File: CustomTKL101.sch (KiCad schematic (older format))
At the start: 223 parts

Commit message: fixed global flags
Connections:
- net DB+ is gone; now on net D+: R?.2
- net DB- is gone; now on net D-: R?.2
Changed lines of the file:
@@
 	4800 8200 4500 8200
 Text GLabel 4500 8200 0    50   Input ~ 0
-DB-
+D-
 $Comp
 L Device:R_Small R?
@@
 	5300 8000 5350 8000
 Text GLabel 4500 8000 0    50   Input ~ 0
-DB+
+D+
 Wire Wire Line
 	4500 8000 4800 8000

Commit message: Board Progress
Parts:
- C1, C2, C3, C4, C5, C6, C7: renamed from C?; footprint (none) -> Capacitor_SMD:C_0805_2012Metric
- D1, D10, D100, D101, D11, D12, D13, D14, D15, D16, D17, D18, D19, D2, D20, D21, D22, D23, D24, D25, D26, D27, D28, D29, D3, D30, D31, D32, D33, D34, D35, D36, D37, D38, D39, D4, D40, D41, D42, D43, D44, D45, D46, D47, D48, D49, D5, D50, D51, D52, D53, D54, D55, D56, D57, D58, D59, D6, D60, D61, D62, D63, D64, D65, D66, D67, D68, D69, D7, D70, D71, D72, D73, D74, D75, D76, D77, D78, D79, D8, D80, D81, D82, D83, D84, D85, D86, D87, D88, D89, D9, D90, D91, D92, D93, D94, D95, D96, D97, D98, D99: renamed from D?; footprint (none) -> Diode_SMD:D_SOD-123
- F1: renamed from F?; footprint (none) -> Fuse:Fuse_1206_3216Metric
- J1: renamed from J?; footprint GCT_USB4085-GF-A_REVA -> USB4085-GF-A_REVA:GCT_USB4085-GF-A_REVA
- MX1, MX10, MX100, MX101, MX11, MX12, MX13, MX14, MX15, MX16, MX17, MX18, MX19, MX2, MX20, MX21, MX22, MX23, MX24, MX25, MX26, MX27, MX28, MX29, MX3, MX30, MX31, MX32, MX33, MX34, MX35, MX36, MX37, MX38, MX39, MX4, MX40, MX41, MX42, MX43, MX44, MX45, MX46, MX47, MX48, MX49, MX5, MX50, MX51, MX52, MX53, MX54, MX55, MX56, MX57, MX58, MX59, MX6, MX60, MX61, MX62, MX63, MX64, MX65, MX66, MX67, MX68, MX69, MX7, MX70, MX71, MX72, MX73, MX74, MX75, MX76, MX77, MX78, MX79, MX8, MX80, MX81, MX82, MX83, MX84, MX85, MX86, MX87, MX88, MX89, MX9, MX90, MX91, MX92, MX93, MX94, MX95, MX96, MX97, MX98, MX99: renamed from MX?; footprint (none) -> MX_Alps_Hybrid:MX-1U-NoLED
- R1, R2, R3, R4, R5, R6, R7, R8, R9: renamed from R?; footprint (none) -> Resistor_SMD:R_0805_2012Metric
- SW1: renamed from SW?; footprint (none) -> random-keyboard-parts:SKQG-1155865
- Y1: renamed from Y?; footprint (none) -> Crystal:Crystal_SMD_3225-4Pin_3.2x2.5mm
- gave numbers to parts that had none: 1

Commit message: Board Complete
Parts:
- removed R2: 1.5k, Resistor_SMD:R_0805_2012Metric, symbol Device:R_Small
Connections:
- net Col0&1: now also U1.41 (PF0)
- net Col10&11: now also U1.12 (PB7)
- net Col12&13: now also U1.22 (PD5)
- net Col14&15: now also U1.21 (PD3)
- net Col16&17: now also U1.20 (PD2)
- net Col18&19: now also U1.19 (PD1)
- net Col2&3: now also U1.8 (PB0)
- net Col20: now also MX36.1 (COL), U1.18 (PD0)
- net Col4&5: now also U1.9 (PB1)
- net Col6&7: now also U1.10 (PB2)
- net Col8&9: now also U1.11 (PB3)
- net GND: now also J1.P1 (SHELL), J1.P2 (SHELL), J1.P3 (SHELL), J1.P4 (SHELL)
- net Row0.1: now also U1.25 (PD4)
- net Row0.2: now also U1.26 (PD6)
- net Row1.1: now also U1.40 (PF1)
- net Row1.2: now also U1.32 (PC7)
- net Row2.1: now also U1.39 (PF4)
- net Row2.2: now also U1.31 (PC6)
- net Row3.1: now also U1.38 (PF5)
- net Row3.2: now also U1.30 (PB6)
- net Row4.1: now also U1.37 (PF6)
- net Row4.2: now also U1.29 (PB5)
- net Row5.1: now also U1.36 (PF7)
- net Row5.2: now also U1.28 (PB4)
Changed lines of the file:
@@
 $EndComp
 Wire Wire Line
-	5150 8700 5350 8700
+	5150 8700 5250 8700
 $Comp
 L Device:R_Small R6
@@
 	1    0    0    -1
 $EndComp
-Connection ~ 4500 7600
-Wire Wire Line
-	4500 7600 4450 7600
-Wire Wire Line
-	4800 7600 4500 7600
-$Comp
-L Device:R_Small R2
-U 1 1 5E4AC4C3
-P 4500 7500
-F 0 "R2" H 4300 7600 50  0000 L CNN
-F 1 "1.5k" H 4300 7500 50  0000 L CNN
-F 2 "Resistor_SMD:R_0805_2012Metric" H 4500 7500 50  0001 C CNN
-F 3 "~" H 4500 7500 50  0001 C CNN
-	1    4500 7500
-	1    0    0    -1
-$EndComp
-$Comp
-L power:+5V #PWR0114
-U 1 1 5E4AFBE5
-P 4500 7400
-F 0 "#PWR0114" H 4500 7250 50  0001 C CNN
-F 1 "+5V" H 4515 7573 50  0000 C CNN
-F 2 "" H 4500 7400 50  0001 C CNN
-F 3 "" H 4500 7400 50  0001 C CNN
-	1    4500 7400
-	1    0    0    -1
-$EndComp
 $Comp
 L power:+5V #PWR0115
@@
 	9900 1400 9900 2450
 Wire Wire Line
-	15100 1150 15100 3200
+	15100 1150 15100 2450
 Wire Wire Line
 	12250 4400 14850 4400
@@
 Wire Wire Line
 	4250 9650 4500 9650
+Wire Wire Line
+	5350 8600 5250 8600
+Wire Wire Line
+	5250 8600 5250 8700
+Connection ~ 5250 8700
+Wire Wire Line
+	5250 8700 5350 8700
+Wire Wire Line
+	4450 7600 4800 7600
+Wire Wire Line
+	15050 2450 15100 2450
+Connection ~ 15100 2450
+Wire Wire Line
+	15100 2450 15100 3200
+Text GLabel 3400 9950 2    50   Input ~ 0
+Col0&1
+Text GLabel 3400 8750 2    50   Input ~ 0
+Col20
+Text GLabel 3400 8850 2    50   Input ~ 0
+Col18&19
+Text GLabel 3400 8950 2    50   Input ~ 0
+Col16&17
+Text GLabel 3400 9050 2    50   Input ~ 0
+Col14&15
+Text GLabel 3400 9250 2    50   Input ~ 0
+Col12&13
+Text GLabel 3400 8250 2    50   Input ~ 0
+Col10&11
+Text GLabel 3400 7850 2    50   Input ~ 0
+Col8&9
+Text GLabel 3400 7750 2    50   Input ~ 0
+Col6&7
+Text GLabel 3400 7650 2    50   Input ~ 0
+Col4&5
+Text GLabel 3400 7550 2    50   Input ~ 0
+Col2&3
+Text GLabel 3500 9750 2    50   Input ~ 0
+NOTOUCH
+Text GLabel 3400 9150 2    50   Input ~ 0
+Row0.1
+Text GLabel 3400 9350 2    50   Input ~ 0
+Row0.2
+Text GLabel 3400 10050 2    50   Input ~ 0
+Row1.1
+Text GLabel 3400 10150 2    50   Input ~ 0
+Row2.1
+Text GLabel 3400 10250 2    50   Input ~ 0
+Row3.1
+Text GLabel 3400 10350 2    50   Input ~ 0
+Row4.1
+Text GLabel 3400 10450 2    50   Input ~ 0
+Row5.1
+Text GLabel 3400 8550 2    50   Input ~ 0
+Row1.2
+Text GLabel 3400 8450 2    50   Input ~ 0
+Row2.2
+Text GLabel 3400 8150 2    50   Input ~ 0
+Row3.2
+Text GLabel 3400 8050 2    50   Input ~ 0
+Row4.2
+Text GLabel 3400 7950 2    50   Input ~ 0
+Row5.2
 $EndSCHEMATC

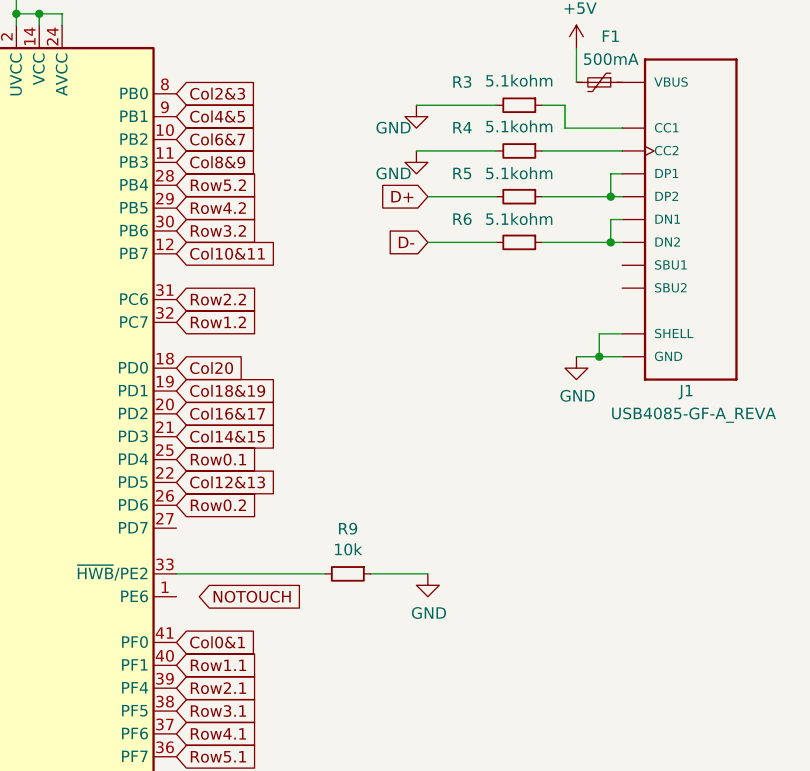
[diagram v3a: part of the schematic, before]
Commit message: Removed dataline resistors
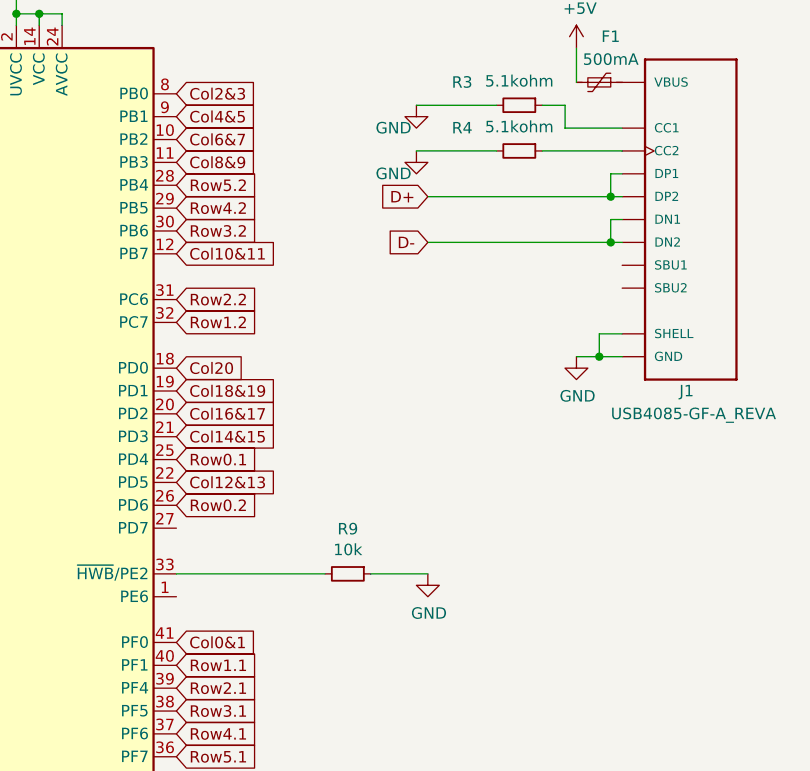
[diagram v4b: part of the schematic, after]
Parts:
- removed R5, R6: 5.1kohm, Resistor_SMD:R_0805_2012Metric, symbol Device:R_Small
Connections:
- net D+: now also J1.A6 (DP1), J1.B6 (DP2)
- net D-: now also J1.A7 (DN1), J1.B7 (DN2)
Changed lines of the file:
@@
 Wire Wire Line
 	5150 8700 5250 8700
-$Comp
-L Device:R_Small R6
-U 1 1 5E496C33
-P 4900 8200
-F 0 "R6" V 4800 7950 50  0000 C CNN
-F 1 "5.1kohm" V 4800 8200 50  0000 C CNN
-F 2 "Resistor_SMD:R_0805_2012Metric" H 4900 8200 50  0001 C CNN
-F 3 "~" H 4900 8200 50  0001 C CNN
-	1    4900 8200
-	0    1    1    0
-$EndComp
-Wire Wire Line
-	5000 8200 5300 8200
 Wire Wire Line
 	5350 8100 5300 8100
@@
 Wire Wire Line
 	5300 8200 5350 8200
-Wire Wire Line
-	4800 8200 4500 8200
 Text GLabel 4500 8200 0    50   Input ~ 0
 D-
-$Comp
-L Device:R_Small R5
-U 1 1 5E49D3FD
-P 4900 8000
-F 0 "R5" V 4800 7750 50  0000 C CNN
-F 1 "5.1kohm" V 4800 8000 50  0000 C CNN
-F 2 "Resistor_SMD:R_0805_2012Metric" H 4900 8000 50  0001 C CNN
-F 3 "~" H 4900 8000 50  0001 C CNN
-	1    4900 8000
-	0    1    1    0
-$EndComp
-Wire Wire Line
-	5000 8000 5300 8000
 Wire Wire Line
 	5350 7900 5300 7900
@@
 Text GLabel 4500 8000 0    50   Input ~ 0
 D+
-Wire Wire Line
-	4500 8000 4800 8000
 $Comp
 L Device:R_Small R4
@@
 Text GLabel 3400 7550 2    50   Input ~ 0
 Col2&3
-Text GLabel 3500 9750 2    50   Input ~ 0
-NOTOUCH
 Text GLabel 3400 9150 2    50   Input ~ 0
 Row0.1
@@
 Text GLabel 3400 7950 2    50   Input ~ 0
 Row5.2
+Wire Wire Line
+	4500 8000 5300 8000
+Wire Wire Line
+	4500 8200 5300 8200
 $EndSCHEMATC

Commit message: Completed PCB ?
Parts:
- MX101, MX32: footprint MX_Alps_Hybrid:MX-1U-NoLED -> MX_Alps_Hybrid:MX-2U-ReversedStabilizers-NoLED
- MX71, MX75: footprint MX_Alps_Hybrid:MX-1U-NoLED -> MX_Alps_Hybrid:MX-2.25U-ReversedStabilizers-NoLED
- MX86: footprint MX_Alps_Hybrid:MX-1U-NoLED -> MX_Alps_Hybrid:MX-2.75U-ReversedStabilizers-NoLED
- MX93: footprint MX_Alps_Hybrid:MX-1U-NoLED -> MX_Alps_Hybrid:MX-6.25U-ReversedStabilizers-NoLED
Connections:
- net Col10&11: now also U1.22 (PD5); no longer U1.12 (PB7)
- net Col12&13: now also U1.27 (PD7); no longer U1.22 (PD5)
- net Col14&15: now also U1.11 (PB3); no longer U1.21 (PD3)
- net Col16&17: now also U1.10 (PB2); no longer U1.20 (PD2)
- net Col18&19: now also U1.9 (PB1); no longer U1.19 (PD1)
- net Col2&3: now also U1.18 (PD0); no longer U1.8 (PB0)
- net Col20: now also U1.8 (PB0); no longer U1.18 (PD0)
- net Col4&5: now also U1.19 (PD1); no longer U1.9 (PB1)
- net Col6&7: now also U1.20 (PD2); no longer U1.10 (PB2)
- net Col8&9: now also U1.21 (PD3); no longer U1.11 (PB3)
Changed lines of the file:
@@
 F 0 "MX93" H 7783 5723 60  0000 C CNN
 F 1 "MX-NoLED" H 7783 5649 20  0000 C CNN
-F 2 "MX_Alps_Hybrid:MX-1U-NoLED" H 7125 5475 60  0001 C CNN
+F 2 "MX_Alps_Hybrid:MX-6.25U-ReversedStabilizers-NoLED" H 7125 5475 60  0001 C CNN
 F 3 "" H 7125 5475 60  0001 C CNN
 	1    7750 5500
@@
 F 0 "MX86" H 11683 4973 60  0000 C CNN
 F 1 "MX-NoLED" H 11683 4899 20  0000 C CNN
-F 2 "MX_Alps_Hybrid:MX-1U-NoLED" H 11025 4725 60  0001 C CNN
+F 2 "MX_Alps_Hybrid:MX-2.75U-ReversedStabilizers-NoLED" H 11025 4725 60  0001 C CNN
 F 3 "" H 11025 4725 60  0001 C CNN
 	1    11650 4750
@@
 F 0 "MX71" H 12333 4223 60  0000 C CNN
 F 1 "MX-NoLED" H 12333 4149 20  0000 C CNN
-F 2 "MX_Alps_Hybrid:MX-1U-NoLED" H 11675 3975 60  0001 C CNN
+F 2 "MX_Alps_Hybrid:MX-2.25U-ReversedStabilizers-NoLED" H 11675 3975 60  0001 C CNN
 F 3 "" H 11675 3975 60  0001 C CNN
 	1    12300 4000
@@
 F 0 "MX32" H 12333 2723 60  0000 C CNN
 F 1 "MX-NoLED" H 12333 2649 20  0000 C CNN
-F 2 "MX_Alps_Hybrid:MX-1U-NoLED" H 11675 2475 60  0001 C CNN
+F 2 "MX_Alps_Hybrid:MX-2U-ReversedStabilizers-NoLED" H 11675 2475 60  0001 C CNN
 F 3 "" H 11675 2475 60  0001 C CNN
 	1    12300 2500
@@
 F 0 "MX101" H 14933 5723 60  0000 C CNN
 F 1 "MX-NoLED" H 14933 5649 20  0000 C CNN
-F 2 "MX_Alps_Hybrid:MX-1U-NoLED" H 14275 5475 60  0001 C CNN
+F 2 "MX_Alps_Hybrid:MX-2U-ReversedStabilizers-NoLED" H 14275 5475 60  0001 C CNN
 F 3 "" H 14275 5475 60  0001 C CNN
 	1    14900 5500
@@
 F 0 "MX75" H 3883 4973 60  0000 C CNN
 F 1 "MX-NoLED" H 3883 4899 20  0000 C CNN
-F 2 "MX_Alps_Hybrid:MX-1U-NoLED" H 3225 4725 60  0001 C CNN
+F 2 "MX_Alps_Hybrid:MX-2.25U-ReversedStabilizers-NoLED" H 3225 4725 60  0001 C CNN
 F 3 "" H 3225 4725 60  0001 C CNN
 	1    3850 4750
@@
 Text GLabel 3400 9950 2    50   Input ~ 0
 Col0&1
-Text GLabel 3400 8750 2    50   Input ~ 0
-Col20
-Text GLabel 3400 8850 2    50   Input ~ 0
-Col18&19
-Text GLabel 3400 8950 2    50   Input ~ 0
-Col16&17
-Text GLabel 3400 9050 2    50   Input ~ 0
-Col14&15
-Text GLabel 3400 9250 2    50   Input ~ 0
-Col12&13
-Text GLabel 3400 8250 2    50   Input ~ 0
-Col10&11
-Text GLabel 3400 7850 2    50   Input ~ 0
-Col8&9
-Text GLabel 3400 7750 2    50   Input ~ 0
-Col6&7
-Text GLabel 3400 7650 2    50   Input ~ 0
-Col4&5
-Text GLabel 3400 7550 2    50   Input ~ 0
-Col2&3
 Text GLabel 3400 9150 2    50   Input ~ 0
 Row0.1
@@
 Wire Wire Line
 	4500 8200 5300 8200
+Text GLabel 3400 7550 2    50   Input ~ 0
+Col20
+Text GLabel 3400 7650 2    50   Input ~ 0
+Col18&19
+Text GLabel 3400 7750 2    50   Input ~ 0
+Col16&17
+Text GLabel 3400 7850 2    50   Input ~ 0
+Col14&15
+Text GLabel 3400 9450 2    50   Input ~ 0
+Col12&13
+Text GLabel 3400 9250 2    50   Input ~ 0
+Col10&11
+Text GLabel 3400 9050 2    50   Input ~ 0
+Col8&9
+Text GLabel 3400 8950 2    50   Input ~ 0
+Col6&7
+Text GLabel 3400 8850 2    50   Input ~ 0
+Col4&5
+Text GLabel 3400 8750 2    50   Input ~ 0
+Col2&3
 $EndSCHEMATC
